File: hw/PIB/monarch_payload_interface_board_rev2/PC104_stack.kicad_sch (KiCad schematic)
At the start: 24 parts, among them U1 Payload, U10 AD7124-8BCPZ-RL, U11 WSK06121L000FEA, U12 WSK06121L000FEA, U13 WSK06121L000FEA

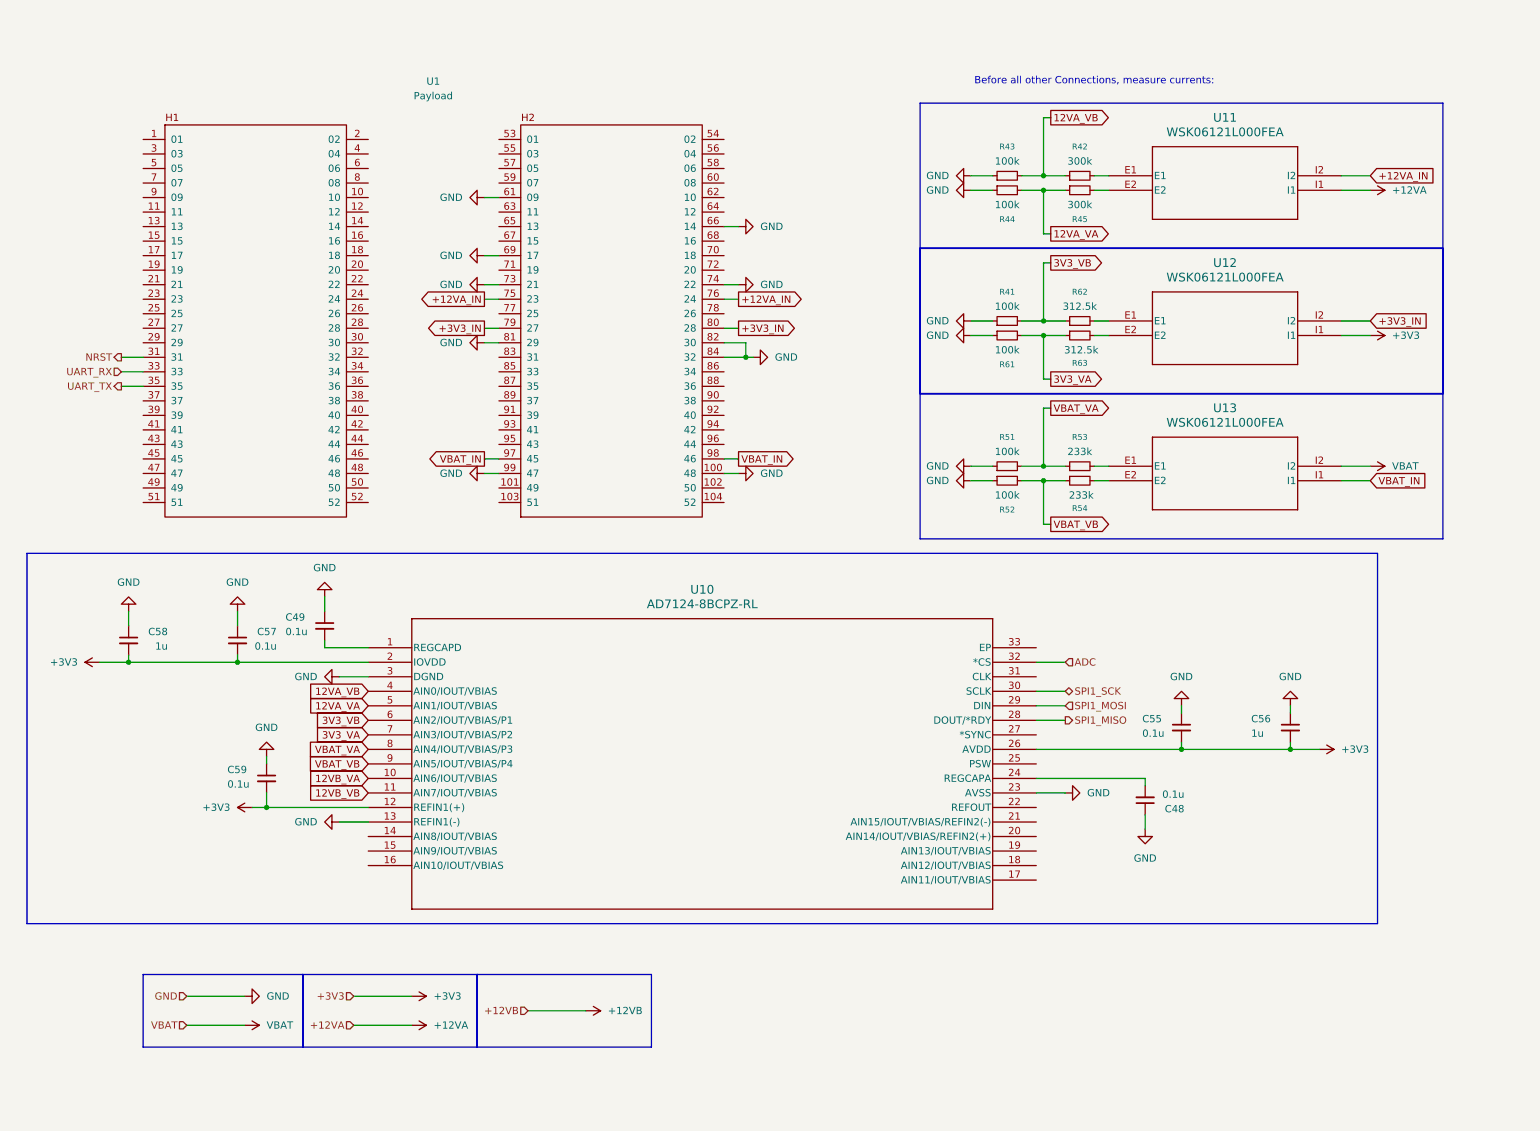
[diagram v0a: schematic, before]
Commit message: Debugging LEDS, Power LEDs, and Button for NRST
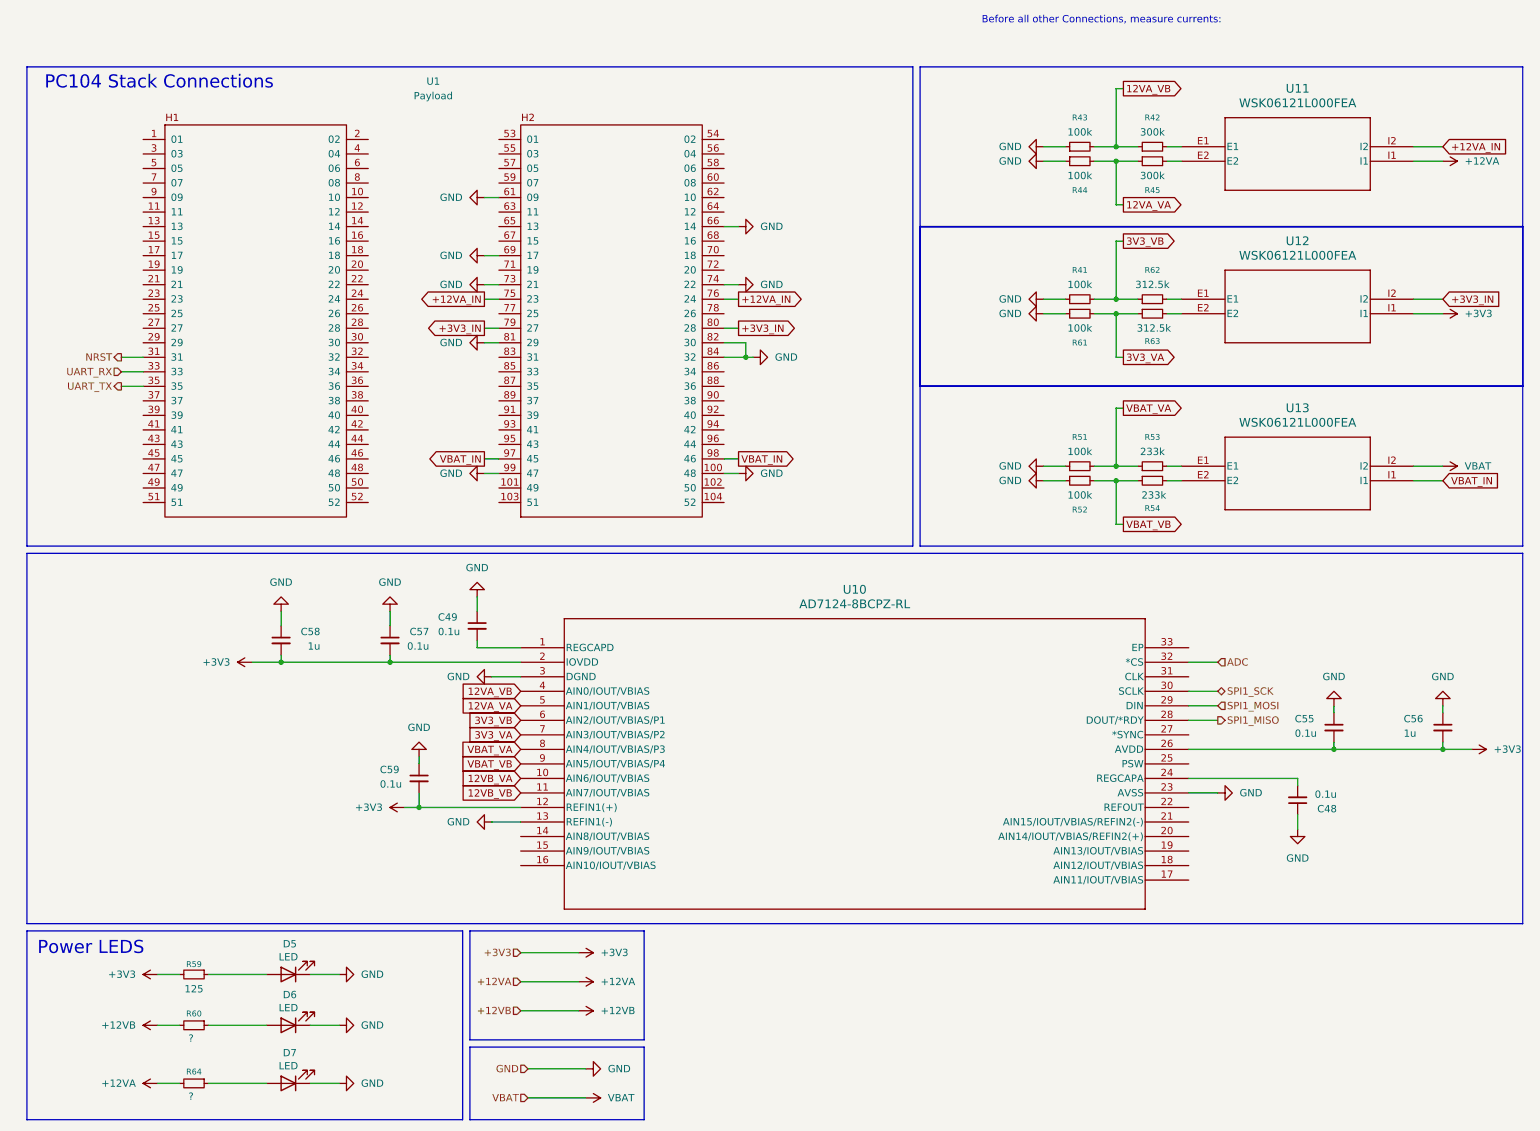
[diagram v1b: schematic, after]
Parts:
- added D5, D6, D7: LED, LED_SMD:LED_0603_1608Metric, symbol Device:LED
- added R59: 125, Resistor_SMD:R_0603_1608Metric, symbol Device:R_Small
- added R60, R64: ?, Resistor_SMD:R_0603_1608Metric, symbol Device:R_Small
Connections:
- net +12VA: now also R64.2
- net +12VB: now also R60.2
- net +3V3: now also R59.2
- net GND: now also D5.1 (K), D6.1 (K), D7.1 (K)
- new net: D7.2 (A), R64.1
- new net: D6.2 (A), R60.1
- new net: D5.2 (A), R59.1
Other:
- note added: "PC104 Stack Connections"
- note added: "Power LEDS"
- moved on the sheet: C48, C49, C55, C56, C57, C58, C59, R41, R42, R43, R44, R45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

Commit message: MCU Power Pins Fix
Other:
- note added: "AD7124-8"
- moved on the sheet: R41, R42, R43, R44, R45, R51, R52, R53, R54, R61, R62, R63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
